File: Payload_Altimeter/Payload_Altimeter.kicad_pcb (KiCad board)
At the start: 2 copper layers, 80 x 93.3 mm, 5 parts, among them J1 L717SDC37P1ACH4F, U1 Arduino_Pro_Mini, U7 MS5607-02BA

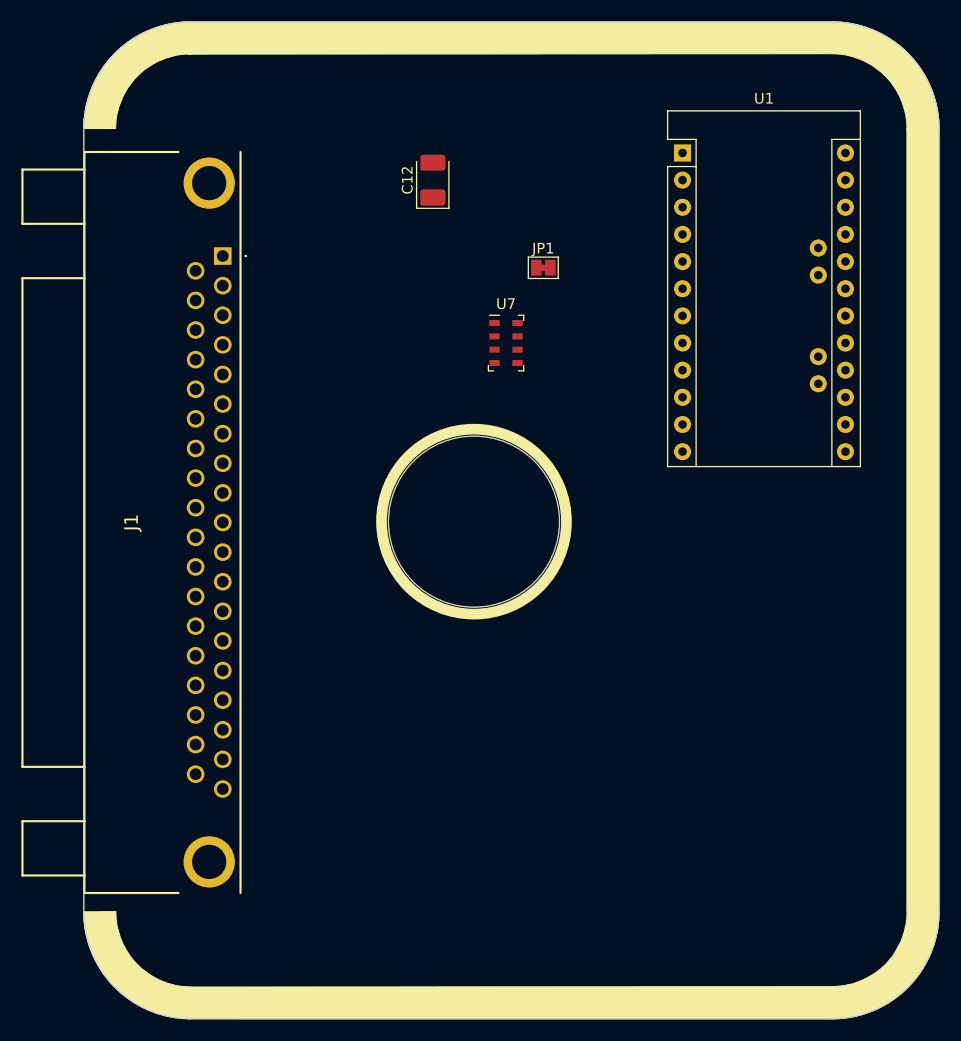
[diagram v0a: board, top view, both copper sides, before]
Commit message: Wired 5V created Arduino Sheet
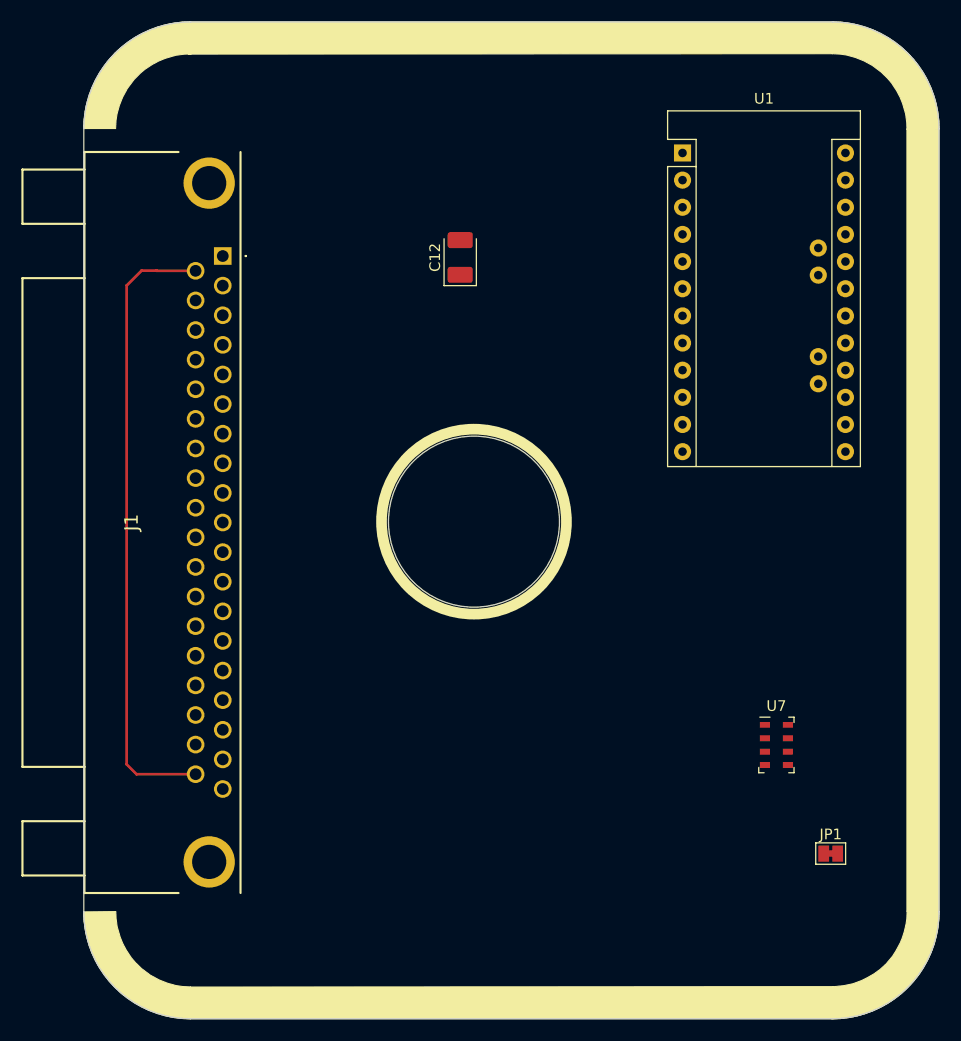
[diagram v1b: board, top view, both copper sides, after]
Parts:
- moved JP1 61.0 mm to (149.9, 129.5)
- moved U7 45.3 mm to (144.8, 119.4)
- moved C12 7.68 mm to (115.2, 73.8)
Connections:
- J1 pad 20: (no net) -> /DSUB/Dsub_5v
- J1 pad 21: (no net) -> /DSUB/t_mosi
- J1 pad 22: (no net) -> /DSUB/t_clk
- J1 pad 23: (no net) -> /DSUB/SWCLK
- J1 pad 24: (no net) -> /Arduino/I2C_SDA
- J1 pad 25: (no net) -> /DSUB/NRST
- J1 pad 26: (no net) -> /DSUB/Fire_redundant
- J1 pad 3: (no net) -> /DSUB/t_miso
- J1 pad 37: (no net) -> /DSUB/Dsub_5v
- J1 pad 4: (no net) -> /DSUB/SWDIO
- J1 pad 5: (no net) -> /Arduino/I2C_SCL
- J1 pad 6: (no net) -> /Arduino/I2C_EN
- J1 pad 7: (no net) -> /DSUB/Fire
- U1 pad 11: unconnected-(U1-Pad11) -> /Arduino/I2C_EN
- U1 pad 13: unconnected-(U1-Pad13) -> /Arduino/SPI_SS
- U1 pad 14: unconnected-(U1-Pad14) -> /Altimeter/SDI_SDA
- U1 pad 15: /Altimeter/PS -> /Altimeter/SDO
- U1 pad 16: unconnected-(U1-Pad16) -> /Altimeter/SCLK
- U1 pad 19: /Altimeter/SDO -> unconnected-(U1-Pad19)
- U1 pad 20: /Altimeter/SCLK -> unconnected-(U1-Pad20)
- U1 pad 7: /DSUB/Alert_scl -> unconnected-(U1-Pad7)
- U1 pad 8: /DSUB/Alert_sda -> unconnected-(U1-Pad8)
- U1 pad A4: unconnected-(U1-PadA4) -> /Arduino/I2C_SDA
- U1 pad A5: unconnected-(U1-PadA5) -> /Arduino/I2C_SCL
- U7 pad 2: /Altimeter/PS -> GND
- U7 pad 4: /Altimeter/~{CSB} -> GND
- U7 pad 5: /Altimeter/~{CSB} -> GND
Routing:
- net /DSUB/Dsub_5v: track 0.00 -> 58.7 mm

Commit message: added sd card
sd card was added and traces were placed for other components
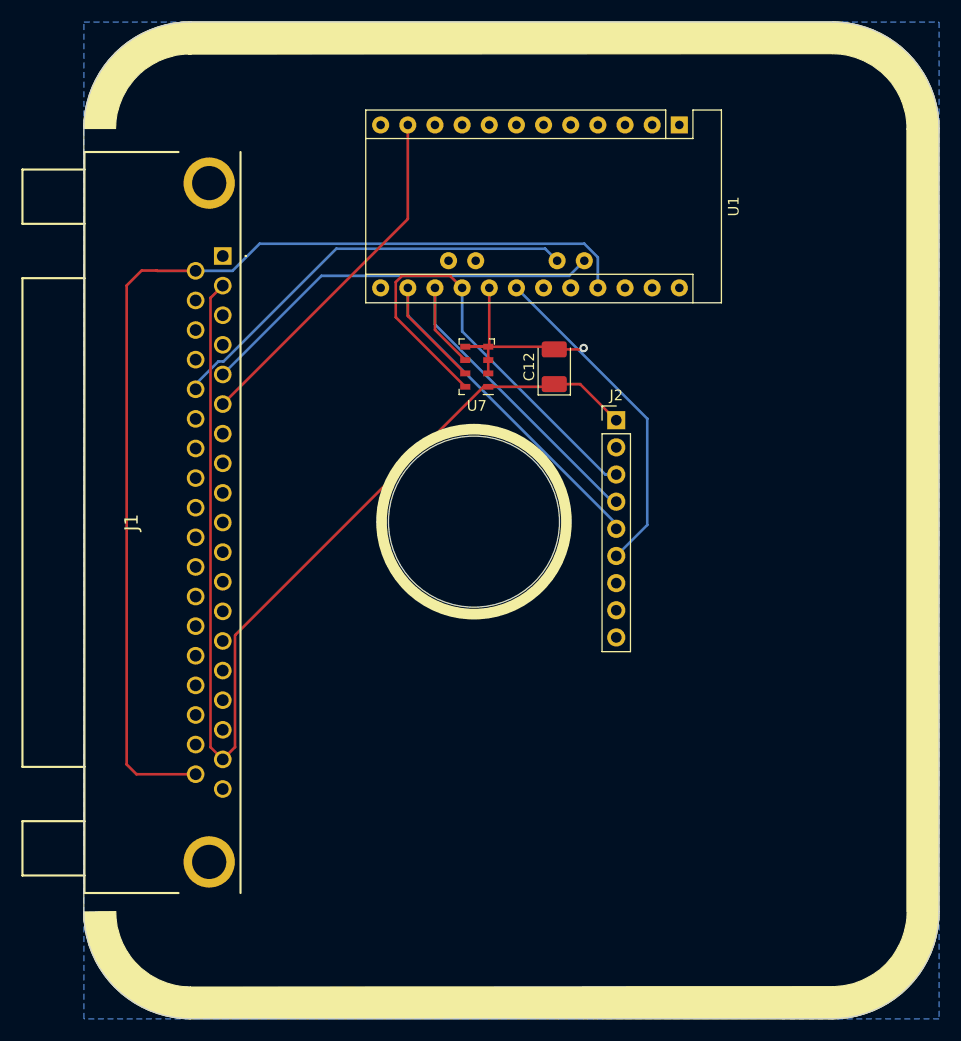
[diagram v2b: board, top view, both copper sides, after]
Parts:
- removed JP1: 5V Disconnect, Jumper:SolderJumper-2_P1.3mm_Bridged_Pad1.0x1.5mm
- added J2: Conn_01x09, Connector_PinHeader_2.54mm:PinHeader_1x09_P2.54mm_Vertical, F.Cu at (129.8, 89.0)
- moved U7 45.1 mm to (116.8, 84.0), turned to 180 degrees
- moved C12 13.5 mm to (124.0, 84.0)
- moved U1 2.64 mm to (135.7, 61.4), turned to -90 degrees
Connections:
- J1 pad 20: /DSUB/Dsub_5v -> +5V
- J1 pad 37: /DSUB/Dsub_5v -> +5V
- U1 pad 17: unconnected-(U1-Pad17) -> /Altimeter/~{CSB}
- U1 pad 18: unconnected-(U1-Pad18) -> /Arduino/sd_cs
- U7 pad 4: GND -> /Altimeter/~{CSB}
- U7 pad 5: GND -> /Altimeter/~{CSB}
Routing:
- net +3V3: track 0.00 -> 104.7 mm
- net +5V: track 0.00 -> 100.7 mm
- net /DSUB/Dsub_5v: track 58.7 -> 0.00 mm
- net /Altimeter/SCLK: track 0.00 -> 43.4 mm
- net /Altimeter/SDI_SDA: track 0.00 -> 40.8 mm
- net /Arduino/I2C_SDA: track 0.00 -> 40.0 mm
- net /Arduino/I2C_SCL: track 0.00 -> 38.2 mm
- net /Altimeter/SDO: track 0.00 -> 35.2 mm
- net /Arduino/I2C_EN: track 0.00 -> 33.3 mm
- net /Arduino/sd_cs: track 0.00 -> 31.4 mm
- net GND: track 0.00 -> 13.7 mm, vias 0 -> 1
- net /Altimeter/~{CSB}: track 0.00 -> 7.69 mm
- added copper zone on B.Cu, net GND

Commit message: Fixed Capacitor
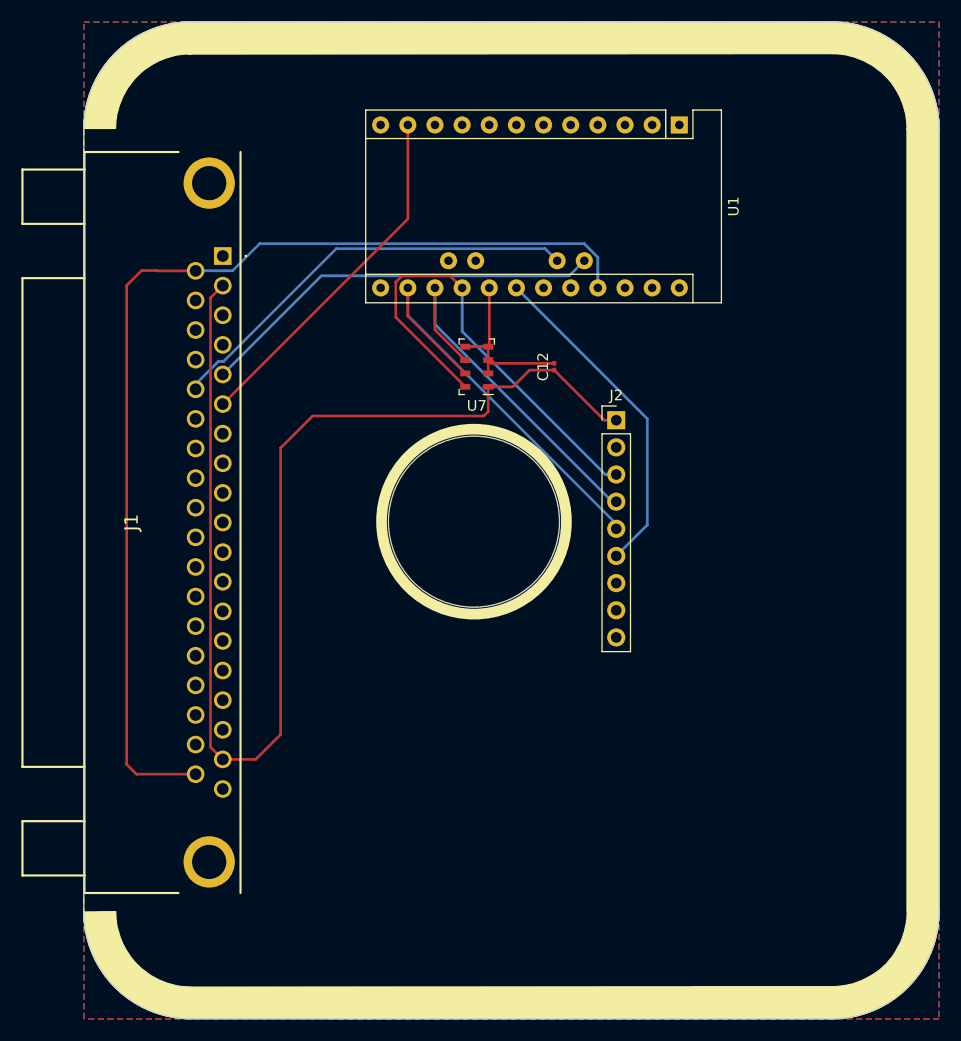
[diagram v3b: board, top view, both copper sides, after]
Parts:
- C12: footprint Capacitor_Tantalum_SMD:CP_EIA-3528-15_AVX-H_Pad1.50x2.35mm_HandSolder -> Capacitor_SMD:C_0201_0603Metric
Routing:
- net +3V3: track 104.7 -> 117.7 mm
- net GND: track 13.7 -> 6.30 mm, vias 1 -> 0
- net /Altimeter/~{CSB}: track 7.69 -> 12.3 mm
- added copper zone on F.Cu, net GND
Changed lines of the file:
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@@
     )
   )
-  (footprint "Capacitor_Tantalum_SMD:CP_EIA-3528-15_AVX-H_Pad1.50x2.35mm_HandSolder" (layer "F.Cu")
+  (footprint "Capacitor_SMD:C_0201_0603Metric" (layer "F.Cu")
     (at 124 84 90)
-    (descr "Tantalum Capacitor SMD AVX-H (3528-15 Metric), IPC_7351 nominal, (Body size from: http://www.kemet.com/Lists/ProductCatalog/Attachments/253/KEM_TC101_STD.pdf), generated with kicad-footprint-generator")
-    (tags "capacitor tantalum")
+    (descr "Capacitor SMD 0201 (0603 Metric), square (rectangular) end terminal, IPC_7351 nominal, (Body size source: https://www.vishay.com/docs/20052/crcw0201e3.pdf), generated with kicad-footprint-generator")
+    (tags "capacitor")
     (property "Sheetfile" "COMPONENT_SHEETS\\BAROMETER_MS5607-02.kicad_sch")
     (property "Sheetname" "Altimeter")
     (attr smd)
-    (fp_text reference "C12" (at 0 -2.35 90) (layer "F.SilkS")
-      (effects (font (size 1 1) (thickness 0.15)))
-    )
-    (fp_text value "100nF" (at 0 2.35 90) (layer "F.Fab")
-      (effects (font (size 1 1) (thickness 0.15)))
-    )
-    (fp_text user "${REFERENCE}" (at 0 0 90) (layer "F.Fab")
-      (effects (font (size 0.88 0.88) (thickness 0.13)))
-    )
-    (fp_line (start -2.635 1.51) (end 1.75 1.51) (layer "F.SilkS") (width 0.12))
-    (fp_line (start -2.635 -1.51) (end -2.635 1.51) (layer "F.SilkS") (width 0.12))
-    (fp_line (start 1.75 -1.51) (end -2.635 -1.51) (layer "F.SilkS") (width 0.12))
-    (fp_line (start -2.62 -1.65) (end 2.62 -1.65) (layer "F.CrtYd") (width 0.05))
-    (fp_line (start 2.62 1.65) (end -2.62 1.65) (layer "F.CrtYd") (width 0.05))
-    (fp_line (start -2.62 1.65) (end -2.62 -1.65) (layer "F.CrtYd") (width 0.05))
-    (fp_line (start 2.62 -1.65) (end 2.62 1.65) (layer "F.CrtYd") (width 0.05))
-    (fp_line (start -1.05 -1.4) (end -1.75 -0.7) (layer "F.Fab") (width 0.1))
-    (fp_line (start -1.75 1.4) (end 1.75 1.4) (layer "F.Fab") (width 0.1))
-    (fp_line (start 1.75 1.4) (end 1.75 -1.4) (layer "F.Fab") (width 0.1))
-    (fp_line (start 1.75 -1.4) (end -1.05 -1.4) (layer "F.Fab") (width 0.1))
-    (fp_line (start -1.75 -0.7) (end -1.75 1.4) (layer "F.Fab") (width 0.1))
-    (pad "1" smd roundrect (at -1.625 0 90) (size 1.5 2.35) (layers "F.Cu" "F.Paste" "F.Mask") (roundrect_rratio 0.166667)
+    (fp_text reference "C12" (at 0 -1.05 90) (layer "F.SilkS")
+      (effects (font (size 1 1) (thickness 0.15)))
+    )
+    (fp_text value "100nF" (at 0 1.05 90) (layer "F.Fab")
+      (effects (font (size 1 1) (thickness 0.15)))
+    )
+    (fp_text user "${REFERENCE}" (at 0 -0.68 90) (layer "F.Fab")
+      (effects (font (size 0.25 0.25) (thickness 0.04)))
+    )
+    (fp_line (start 0.7 -0.35) (end 0.7 0.35) (layer "F.CrtYd") (width 0.05))
+    (fp_line (start -0.7 0.35) (end -0.7 -0.35) (layer "F.CrtYd") (width 0.05))
+    (fp_line (start -0.7 -0.35) (end 0.7 -0.35) (layer "F.CrtYd") (width 0.05))
+    (fp_line (start 0.7 0.35) (end -0.7 0.35) (layer "F.CrtYd") (width 0.05))
+    (fp_line (start 0.3 0.15) (end -0.3 0.15) (layer "F.Fab") (width 0.1))
+    (fp_line (start -0.3 -0.15) (end 0.3 -0.15) (layer "F.Fab") (width 0.1))
+    (fp_line (start -0.3 0.15) (end -0.3 -0.15) (layer "F.Fab") (width 0.1))
+    (fp_line (start 0.3 -0.15) (end 0.3 0.15) (layer "F.Fab") (width 0.1))
+    (pad "" smd roundrect (at -0.345 0 90) (size 0.318 0.36) (layers "F.Paste") (roundrect_rratio 0.25))
+    (pad "" smd roundrect (at 0.345 0 90) (size 0.318 0.36) (layers "F.Paste") (roundrect_rratio 0.25))
+    (pad "1" smd roundrect (at -0.32 0 90) (size 0.46 0.4) (layers "F.Cu" "F.Mask") (roundrect_rratio 0.25)
       (net 1 "+3V3") (pintype "passive"))
-    (pad "2" smd roundrect (at 1.625 0 90) (size 1.5 2.35) (layers "F.Cu" "F.Paste" "F.Mask") (roundrect_rratio 0.166667)
+    (pad "2" smd roundrect (at 0.32 0 90) (size 0.46 0.4) (layers "F.Cu" "F.Mask") (roundrect_rratio 0.25)
       (net 2 "GND") (pintype "passive"))
-    (model "${KICAD6_3DMODEL_DIR}/Capacitor_Tantalum_SMD.3dshapes/CP_EIA-3528-15_AVX-H.wrl"
+    (model "${KICAD6_3DMODEL_DIR}/Capacitor_SMD.3dshapes/C_0201_0603Metric.wrl"
       (offset (xyz 0 0 0))
       (scale (xyz 1 1 1))
@@
   (target plus (at 81.98989 141.91489) (size 2) (width 0.05) (layer "Edge.Cuts"))
   (target plus (at 79.98989 144.98989) (size 5) (width 0.05) (layer "Edge.Cuts"))
-  (segment (start 94.139401 119.580379) (end 94.139401 109.110599) (width 0.25) (layer "F.Cu") (net 1))
-  (segment (start 126.425 85.625) (end 129.8 89) (width 0.25) (layer "F.Cu") (net 1))
-  (segment (start 94.139401 109.110599) (end 117.375 85.875) (width 0.25) (layer "F.Cu") (net 1))
-  (segment (start 124 85.625) (end 123.75 85.875) (width 0.25) (layer "F.Cu") (net 1))
+  (segment (start 117.825 85.875) (end 117.825 88.175) (width 0.25) (layer "F.Cu") (net 1))
+  (segment (start 117.825 88.175) (end 117.4 88.6) (width 0.25) (layer "F.Cu") (net 1))
   (segment (start 118.375 85.875) (end 117.825 85.875) (width 0.25) (layer "F.Cu") (net 1))
-  (segment (start 124 85.625) (end 126.425 85.625) (width 0.25) (layer "F.Cu") (net 1))
+  (segment (start 117.4 88.6) (end 101.4 88.6) (width 0.25) (layer "F.Cu") (net 1))
+  (segment (start 120.125 85.875) (end 121.68 84.32) (width 0.25) (layer "F.Cu") (net 1))
+  (segment (start 117.825 85.875) (end 120.125 85.875) (width 0.25) (layer "F.Cu") (net 1))
   (segment (start 117.375 85.875) (end 118.375 85.875) (width 0.25) (layer "F.Cu") (net 1))
-  (segment (start 123.75 85.875) (end 118.375 85.875) (width 0.25) (layer "F.Cu") (net 1))
+  (segment (start 98.4 118.4) (end 96.07011 120.72989) (width 0.25) (layer "F.Cu") (net 1))
+  (segment (start 128.68 89) (end 129.8 89) (width 0.25) (layer "F.Cu") (net 1))
+  (segment (start 121.68 84.32) (end 124 84.32) (width 0.25) (layer "F.Cu") (net 1))
+  (segment (start 124 84.32) (end 128.68 89) (width 0.25) (layer "F.Cu") (net 1))
+  (segment (start 96.07011 120.72989) (end 92.98989 120.72989) (width 0.25) (layer "F.Cu") (net 1))
+  (segment (start 101.4 88.6) (end 98.4 91.6) (width 0.25) (layer "F.Cu") (net 1))
   (segment (start 91.840379 119.580379) (end 92.98989 120.72989) (width 0.25) (layer "F.Cu") (net 1))
   (segment (start 91.840379 77.559401) (end 91.840379 119.580379) (width 0.25) (layer "F.Cu") (net 1))
-  (segment (start 92.98989 120.72989) (end 94.139401 119.580379) (width 0.25) (layer "F.Cu") (net 1))
   (segment (start 92.98989 76.40989) (end 91.840379 77.559401) (width 0.25) (layer "F.Cu") (net 1))
-  (segment (start 117.825 82.125) (end 117.825 83.375) (width 0.25) (layer "F.Cu") (net 2))
-  (segment (start 115.675 82.125) (end 117.825 82.125) (width 0.25) (layer "F.Cu") (net 2))
-  (segment (start 117.825 83.375) (end 117.825 84.625) (width 0.25) (layer "F.Cu") (net 2))
-  (segment (start 117.825 82.125) (end 123.75 82.125) (width 0.25) (layer "F.Cu") (net 2))
-  (segment (start 123.75 82.125) (end 124 82.375) (width 0.25) (layer "F.Cu") (net 2))
-  (segment (start 126.625 82.375) (end 126.75 82.25) (width 0.25) (layer "F.Cu") (net 2))
-  (segment (start 124 82.375) (end 126.625 82.375) (width 0.25) (layer "F.Cu") (net 2))
-  (via (at 126.75 82.25) (size 0.8) (drill 0.4) (layers "F.Cu" "B.Cu") (free) (net 2))
+  (segment (start 98.4 91.6) (end 98.4 118.4) (width 0.25) (layer "F.Cu") (net 1))
+  (segment (start 124 83.68) (end 118.13 83.68) (width 0.25) (layer "F.Cu") (net 2))
+  (segment (start 118.13 83.68) (end 117.825 83.375) (width 0.25) (layer "F.Cu") (net 2))
   (segment (start 84 121.2) (end 84 76.4) (width 0.25) (layer "F.Cu") (net 3))
   (segment (start 84.91489 122.11489) (end 84 121.2) (width 0.25) (layer "F.Cu") (net 3))
@@
   (segment (start 103.609946 72.955489) (end 93.065435 83.5) (width 0.25) (layer "B.Cu") (net 50))
   (segment (start 92.584125 83.5) (end 90.44989 85.634235) (width 0.25) (layer "B.Cu") (net 50))
+  (segment (start 117.825 82.125) (end 117.825 83.375) (width 0.25) (layer "F.Cu") (net 60))
+  (segment (start 115.675 82.125) (end 117.825 82.125) (width 0.25) (layer "F.Cu") (net 60))
+  (segment (start 117.825 83.375) (end 117.825 84.625) (width 0.25) (layer "F.Cu") (net 60))
   (segment (start 117.825 82.125) (end 117.92 82.03) (width 0.25) (layer "F.Cu") (net 60))
   (segment (start 115.675 82.125) (end 117.825 82.125) (width 0.25) (layer "F.Cu") (net 60))
   (segment (start 117.92 82.03) (end 117.92 76.62) (width 0.25) (layer "F.Cu") (net 60))
+  (zone (net 2) (net_name "GND") (layer "F.Cu") (hatch edge 0.508)
+    (connect_pads (clearance 0.508))
+    (min_thickness 0.254) (filled_areas_thickness no)
+    (fill yes (thermal_gap 0.508) (thermal_bridge_width 0.508))
+    (polygon
+      (pts
+        (xy 160 145)
+        (xy 80 145)
+        (xy 80 51.75)
+        (xy 160 51.75)
+      )
+    )
+  )
   (zone (net 2) (net_name "GND") (layer "B.Cu") (hatch edge 0.508)
     (connect_pads (clearance 0.508))
